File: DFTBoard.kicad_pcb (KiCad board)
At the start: 8 copper layers, 148.5 x 62 mm, 76 parts, among them CON1 AVR-JTAG-10, CON2 AVR-JTAG-10, J1 AUDIO JACK, J2 JACK_TRS_4PINS, J3 AUDIO JACK, J4 AUDIO JACK, J5 USB_A, J6 Micro_SD_Card_Det, SW1 TL6215RF200BDT, U10 APDS-9960, U11 W9751G6KB, U12 W9751G6KB, U7 TLV320AIC3104, U9 VL53L0X

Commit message: passes ERC, about to update footprints to v5 references
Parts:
- removed C63, C67: 10uF, Capacitors_SMD:C_0603
- removed C71, C73: .1uF, Capacitors_SMD:C_0603
- removed C79: 47uF, Capacitors_SMD:C_1210
- removed C80: 4.7uF, Capacitors_SMD:C_0603
- removed D4: LED_RGB, DFTcustom:PLCC6-SM-RGB-LED
- removed NCP1: NCP361, DFTcustom:TSOP-5
- removed R24: 10k, Resistors_SMD:R_0402
- removed the U11 at (196.0, 104.1)
- added C76: 18pF, Capacitor_SMD:C_0402_1005Metric, F.Cu at (223.2, 39.6)
- added C77: 18pF, Capacitor_SMD:C_0402_1005Metric, F.Cu at (223.2, 41.6)
- added C85: 18pF, Capacitor_SMD:C_0402_1005Metric, F.Cu at (225.1, 40.6)
- added C86: 18pF, Capacitor_SMD:C_0402_1005Metric, F.Cu at (230.6, 36.5)
- added D1: LED_RGB, DFTcustom:PLCC6-SM-RGB-LED, F.Cu at (224.6, 117.8)
- added D2: LED_RGB, DFTcustom:PLCC6-SM-RGB-LED, F.Cu at (149.2, 122.5)
- added J7: USB_B, Connector_USB:USB_B_Amphenol_MUSB-D511_Vertical_Rugged, F.Cu at (245.2, 139.8)
- added R27: 1M, Resistor_SMD:R_0402_1005Metric, F.Cu at (223.2, 40.6)
- added R29: 8.06k 1%, Resistor_SMD:R_0402_1005Metric, F.Cu at (225.1, 39.6)
- added R34: 1M, Resistor_SMD:R_0402_1005Metric, F.Cu at (240.7, 25.5)
- added R35: 8.06k 1%, Resistor_SMD:R_0402_1005Metric, F.Cu at (230.6, 35.5)
- added R40: 240 1%, Resistor_SMD:R_0402_1005Metric, F.Cu at (201.2, 99.9)
- added R43: 240 1%, Resistor_SMD:R_0402_1005Metric, F.Cu at (203.1, 99.9)
- added R45: 80.6, Resistor_SMD:R_0402_1005Metric, F.Cu at (205.0, 99.9)
- added R46: 80.6, Resistor_SMD:R_0402_1005Metric, F.Cu at (206.9, 99.9)
- added U13: MT41K256M16HA-125_E, DFTcustom:FBGA-96-DDR3-SDRAM, F.Cu at (195.2, 107.5)
- added U5: xc7z020clg400, Package_BGA:BGA-400_21.0x21.0mm_Layout20x20_P1.0mm, F.Cu at (189.9, 134.3)
- added U9: MIC2025-1YMM, Crystal:Crystal_HC35-U, F.Cu at (214.7, 44.1)
- added Y1: Crystal, Crystal:Crystal_HC35-U, F.Cu at (232.2, 30.0)
- added Y2: Crystal, Crystal:Crystal_HC35-U, F.Cu at (204.7, 44.1)
- R41: renamed from R23; value 10k -> 10k 1%
- U12: value W9751G6KB -> MT41K256M16HA-125_E; footprint DFTcustom:WBGA-84 -> DFTcustom:FBGA-96-DDR3-SDRAM
- moved CONN1 125.5 mm to (170.8, 102.2), turned to 270 degrees
- moved J6 63.9 mm to (242.7, 118.7), turned to 90 degrees
- moved CON1 42.6 mm to (211.2, 156.5)
- moved GT1 22.8 mm to (178.8, 163.8)
- moved CON2 18.1 mm to (220.2, 160.1)
- moved U12 10.1 mm to (185.0, 107.5)
- renumbered C81 to C102, C82 to C104, C83 to C105, C84 to C106, C85 to C107, C34 to C35, C35 to C36, C36 to C39, C37 to C40, C38 to C41, C39 to C43, C40 to C44, C41 to C46, C42 to C50, C43 to C51, C44 to C52, C45 to C53, C46 to C54, C47 to C55, C48 to C56, C49 to C57, C50 to C58, C51 to C59, C52 to C60, C53 to C61, C54 to C62, C58 to C89, C59 to C90, C60 to C91, C61 to C92, C62 to C93, C65 to C94, C66 to C95, C75 to C96, C76 to C97, J6 to J5, J5 to J6, R1 to R13, R2 to R14, R3 to R15, R4 to R16, R5 to R17, R6 to R18, R7 to R19, R8 to R20, R9 to R21, R10 to R22, R19 to R36, R20 to R37, R27 to R44, U9 to U10, U10 to U11, U7 to U6
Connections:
- C102 pad 1: +1.8V -> Net-(C100-Pad1)
- C104 pad 1: +1.8V -> Net-(C100-Pad1)
- C105 pad 1: +1.8V -> Net-(C100-Pad1)
- C106 pad 1: +1.8V -> Net-(C100-Pad1)
- C107 pad 1: +1.8V -> Net-(C100-Pad1)
- C94 pad 1: +1.8V -> +1V35
- C96 pad 1: +1.8V -> +1V35
- CON1 pad 1: (no net) -> AX_TCLK
- CON1 pad 3: (no net) -> AX_TDO
- CON1 pad 5: (no net) -> AX_TMS
- CON1 pad 9: (no net) -> AX_TDI
- CONN2 pad 10: (no net) -> LCD_RST
- CONN2 pad 11: (no net) -> RGB_VSYNC
- CONN2 pad 12: (no net) -> RGB_HSYNC
- CONN2 pad 13: (no net) -> RGB_DOTCLK
- CONN2 pad 14: (no net) -> RGB_DE
- CONN2 pad 15: (no net) -> LCD_D17
- CONN2 pad 16: (no net) -> LCD_D16
- CONN2 pad 17: (no net) -> LCD_D15
- CONN2 pad 18: (no net) -> LCD_D14
- CONN2 pad 19: (no net) -> LCD_D13
- CONN2 pad 20: (no net) -> LCD_D12
- CONN2 pad 21: (no net) -> LCD_D11
- CONN2 pad 22: (no net) -> LCD_D10
- CONN2 pad 23: (no net) -> LCD_D9
- CONN2 pad 24: (no net) -> LCD_D8
- CONN2 pad 25: (no net) -> LCD_D7
- CONN2 pad 26: (no net) -> LCD_D6
- CONN2 pad 27: (no net) -> LCD_D5
- CONN2 pad 28: (no net) -> LCD_D4
- CONN2 pad 29: (no net) -> LCD_D3
- CONN2 pad 30: (no net) -> LCD_D2
- CONN2 pad 31: (no net) -> LCD_D1
- CONN2 pad 32: (no net) -> LCD_D0
- CONN2 pad 33: (no net) -> LCD_SDO
- CONN2 pad 34: (no net) -> LCD_SDI
- CONN2 pad 35: (no net) -> LCD_READ
- CONN2 pad 36: (no net) -> LCD_WRITE
- CONN2 pad 37: (no net) -> LCD_DorI
- CONN2 pad 38: (no net) -> LCD_CS
- CONN2 pad 39: (no net) -> LCD_TE
- CONN2 pad 6: (no net) -> LCD_IM0
- CONN2 pad 7: (no net) -> LCD_IM1
- CONN2 pad 8: (no net) -> LCD_IM2
- CONN2 pad 9: (no net) -> LCD_IM3
- J5 pad 1: (no net) -> SD_D2
- J5 pad 2: (no net) -> SD_D3
- J5 pad 3: (no net) -> SD_CMD
- J5 pad 5: (no net) -> SD_CLK
- J5 pad 7: (no net) -> SD_D0
- J5 pad 8: (no net) -> SD_D1
- J5 pad 9: (no net) -> SD_CD
- J6 pad 1: SPIUSB_VBUS -> (no net)
- R21 pad 1: I2C_SCLK -> I2C3v3_SCLK
- R21 pad 2: +1.8V -> +3V3
- R22 pad 1: I2C_SDIN -> I2C3v3_SDIN
- R22 pad 2: +1.8V -> +3V3
- R41 pad 1: +1.8V -> +1V35
- SW1 pad 2: (no net) -> TEMPO_SW
- U10 pad 10: I2C_SCLK -> (no net)
- U10 pad 9: I2C_SDIN -> (no net)
- U11 pad 1: I2C_SDIN -> (no net)
- U11 pad 2: (no net) -> RF2_IRQ
- U11 pad 7: I2C_SCLK -> (no net)
- U12 pad A1: +1.8V -> +1V35
- U12 pad A2: (no net) -> DDR3_DQ29
- U12 pad A3: GND -> DDR3_DQ31
- U12 pad A7: GND -> DDR3_DQ28
- U12 pad A8: (no net) -> +1V35
- U12 pad A9: +1.8V -> GND
- U12 pad B1: (no net) -> GND
- U12 pad B2: GND -> +1V35
- U12 pad B3: (no net) -> GND
- U12 pad B7: (no net) -> DDR3_DQS3_N
- U12 pad B8: GND -> DDR3_DQ30
- U12 pad B9: (no net) -> GND
- U12 pad C1: +1.8V -> +1V35
- U12 pad C2: (no net) -> DDR3_DQ27
- U12 pad C3: +1.8V -> DDR3_DQ25
- U12 pad C7: +1.8V -> DDR3_DQS3_P
- U12 pad C8: (no net) -> DDR3_DQ26
- U12 pad C9: +1.8V -> +1V35
- U12 pad D1: (no net) -> GND
- U12 pad D2: GND -> +1V35
- U12 pad D3: (no net) -> DDR3_DM3
- U12 pad D7: (no net) -> DDR3_DQ24
- U12 pad D9: (no net) -> +1V35
- U12 pad E1: +1.8V -> GND
- U12 pad E2: (no net) -> GND
- U12 pad E3: GND -> DDR3_DQ16
- U12 pad E7: GND -> DDR3_DM2
- U12 pad E8: (no net) -> GND
- U12 pad E9: +1.8V -> +1V35
- U12 pad F1: (no net) -> +1V35
- U12 pad F2: GND -> DDR3_DQ18
- U12 pad F3: (no net) -> DDR3_DQS2_P
- U12 pad F7: (no net) -> DDR3_DQ17
- U12 pad F8: GND -> DDR3_DQ19
- U12 pad F9: (no net) -> GND
- U12 pad G1: +1.8V -> GND
- U12 pad G2: (no net) -> DDR3_DQ22
- U12 pad G3: +1.8V -> DDR3_DQS2_N
- U12 pad G7: +1.8V -> +1V35
- U12 pad G8: (no net) -> GND
- U12 pad G9: +1.8V -> GND
- U12 pad H1: (no net) -> /DDR3/VREF
- U12 pad H2: GND -> +1V35
- U12 pad H3: (no net) -> DDR3_DQ20
- U12 pad H7: (no net) -> DDR3_DQ23
- U12 pad H8: GND -> DDR3_DQ21
- U12 pad H9: (no net) -> +1V35
- U12 pad J1: +1.8V -> (no net)
- U12 pad J2: /DDR3/VREF -> GND
- U12 pad J3: GND -> DDR3_RAS#
- U12 pad J7: GND -> DDR3_CK_P
- U12 pad J8: DDR3_CK_P -> GND
- U12 pad J9: +1.8V -> (no net)
- U12 pad K2: DDR3_CKE -> +1V35
- U12 pad K3: DDR3_WE# -> DDR3_CAS#
- U12 pad K7: DDR3_RAS# -> DDR3_CK_N
- U12 pad K8: DDR3_CK_N -> +1V35
- U12 pad K9: DDR3_ODT -> DDR3_CKE
- U12 pad L2: DDR3_BA0 -> DDR3_CS#
- U12 pad L3: DDR3_BA1 -> DDR3_WE#
- U12 pad L7: DDR3_CAS# -> DDR3_A10
- U12 pad L8: DDR3_CS -> Net-(R40-Pad1)
- U12 pad M2: DDR3_A10 -> DDR3_BA0
- U12 pad M3: DDR3_A1 -> DDR3_BA2
- U12 pad M7: DDR3_A2 -> (no net)
- U12 pad M8: DDR3_A0 -> /DDR3/VREF
- U12 pad M9: +1.8V -> GND
- U12 pad N1: GND -> +1V35
- U12 pad N3: DDR3_A5 -> DDR3_A0
- U12 pad N7: DDR3_A6 -> DDR3_A12
- U12 pad N8: DDR3_A4 -> DDR3_BA1
- U12 pad P2: DDR3_A7 -> DDR3_A5
- U12 pad P3: DDR3_A9 -> DDR3_A2
- U12 pad P7: DDR3_A11 -> DDR3_A1
- U12 pad P8: DDR3_A8 -> DDR3_A4
- U12 pad R1: +1.8V -> +1V35
- U12 pad R2: DDR3_A12 -> DDR3_A7
- U12 pad R3: (no net) -> DDR3_A9
- U12 pad R7: (no net) -> DDR3_A11
- U12 pad R8: (no net) -> DDR3_A6
- U6 pad 1: (no net) -> I2S_MCLK
- U6 pad 2: (no net) -> I2S_BCLK
- U6 pad 3: (no net) -> I2S_LRCLK
- U6 pad 4: (no net) -> I2S_DACSD
- U6 pad 5: (no net) -> I2S_ADCSD

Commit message: random updates
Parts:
- removed CON2: AVR-JTAG-10, DFTcustom:XilinxJTAG
- removed the J5 at (247.8, 103.2)
- removed the R37 at (143.6, 128.4)
- removed the R40 at (201.2, 99.9)
- removed the R41 at (205.0, 102.6)
- removed the U13 at (195.2, 107.5)
- added C1: .47uF, Capacitor_SMD:C_0402_1005Metric, B.Cu at (165.2, 141.2)
- added C10: 10uF, Capacitor_SMD:C_0603_1608Metric, F.Cu at (160.0, 96.5)
- added C100: 4.7uF, Capacitor_SMD:C_0402_1005Metric, F.Cu at (217.1, 117.4)
- added C101: .47uF, Capacitor_SMD:C_0402_1005Metric, B.Cu at (185.4, 112.8)
- added C103: .47uF, Capacitor_SMD:C_0402_1005Metric, B.Cu at (191.4, 114.8)
- added C108: 4.7uF, Capacitor_SMD:C_0402_1005Metric, B.Cu at (134.8, 145.1)
- added C109: .1uF, Capacitor_SMD:C_0402_1005Metric, F.Cu at (150.4, 138.4)
- added C11: 10uF, Capacitor_SMD:C_0603_1608Metric, B.Cu at (165.2, 150.8)
- added C110: 4.7uF, Capacitor_SMD:C_0402_1005Metric, B.Cu at (150.4, 138.4)
- added C111: .1uF, Capacitor_SMD:C_0402_1005Metric, B.Cu at (150.4, 136.2)
- added C112: 4.7uF, Capacitor_SMD:C_0402_1005Metric, F.Cu at (150.4, 136.2)
- added C113: 47uF, Capacitor_SMD:C_1210_3225Metric, F.Cu at (176.2, 130.5)
- added C114: 4.7uF, Capacitor_SMD:C_0402_1005Metric, F.Cu at (230.4, 170.4)
- added C115: 4.7uF, Capacitor_SMD:C_0402_1005Metric, B.Cu at (216.4, 130.5)
- added C116: .47uF, Capacitor_SMD:C_0402_1005Metric, B.Cu at (198.0, 127.4)
- added C117: .47uF, Capacitor_SMD:C_0402_1005Metric, F.Cu at (232.3, 170.4)
- added C118: .47uF, Capacitor_SMD:C_0402_1005Metric, F.Cu at (230.4, 172.4)
- added C119: .47uF, Capacitor_SMD:C_0402_1005Metric, B.Cu at (199.4, 125.2)
- added C12: 100uF, Capacitor_SMD:C_1210_3225Metric, F.Cu at (214.1, 135.2)
- added C120: .01uF, Capacitor_SMD:C_0402_1005Metric, B.Cu at (218.2, 120.7)
- added C121: .47uF, Capacitor_SMD:C_0402_1005Metric, B.Cu at (210.2, 130.0)
- added C122: 4.7uF, Capacitor_SMD:C_0402_1005Metric, B.Cu at (208.4, 124.0)
- added C123: 100uF, Capacitor_SMD:C_1210_3225Metric, F.Cu at (216.4, 126.8)
- added C13: 10uF, Capacitor_SMD:C_0603_1608Metric, F.Cu at (154.0, 147.2)
- added C14: .47uF, Capacitor_SMD:C_0402_1005Metric, F.Cu at (218.3, 171.4)
- added C15: .47uF, Capacitor_SMD:C_0402_1005Metric, B.Cu at (202.6, 130.0)
- added C16: 10uF, Capacitor_SMD:C_0603_1608Metric, F.Cu at (244.0, 101.5)
- added C17: .47uF, Capacitor_SMD:C_0402_1005Metric, F.Cu at (220.2, 170.4)
- added C18: .47uF, Capacitor_SMD:C_0402_1005Metric, B.Cu at (197.2, 129.6)
- added C19: 4.7uF, Capacitor_SMD:C_0402_1005Metric, F.Cu at (171.2, 125.7)
- added C2: 10uF, Capacitor_SMD:C_0603_1608Metric, F.Cu at (168.8, 152.2)
- added C20: 4.7uF, Capacitor_SMD:C_0402_1005Metric, B.Cu at (201.6, 129.2)
- added C21: 10uF, Capacitor_SMD:C_0603_1608Metric, F.Cu at (238.0, 103.6)
- added C22: 330uF, Capacitor_SMD:C_1206_3216Metric, F.Cu at (218.4, 137.0)
- added C23: .47uF, Capacitor_SMD:C_0402_1005Metric, B.Cu at (197.2, 126.4)
- added C24: 4.7uF, Capacitor_SMD:C_0402_1005Metric, F.Cu at (204.6, 140.2)
- added C25: 100uF, Capacitor_SMD:C_1210_3225Metric, F.Cu at (176.2, 119.5)
- added C26: 10uF, Capacitor_SMD:C_0603_1608Metric, B.Cu at (161.2, 142.5)
- added C27: 4.7uF, Capacitor_SMD:C_0402_1005Metric, B.Cu at (215.3, 130.5)
- added C28: 100uF, Capacitor_SMD:C_1210_3225Metric, F.Cu at (176.2, 125.5)
- added C29: .47uF, Capacitor_SMD:C_0402_1005Metric, B.Cu at (203.6, 125.8)
- added C3: 10uF, Capacitor_SMD:C_0603_1608Metric, B.Cu at (164.6, 104.1)
- added C30: .47uF, Capacitor_SMD:C_0402_1005Metric, B.Cu at (203.6, 124.8)
- added C31: .47uF, Capacitor_SMD:C_0402_1005Metric, B.Cu at (197.2, 130.6)
- added C32: 47uF, Capacitor_SMD:C_0805_2012Metric, B.Cu at (178.4, 136.4)
- added C33: 10uF, Capacitor_SMD:C_0603_1608Metric, B.Cu at (214.0, 127.8)
- added C34: .47uF, Capacitor_SMD:C_0402_1005Metric, F.Cu at (220.2, 174.4)
- added C37: 1uF, Capacitor_SMD:C_0402_1005Metric, F.Cu at (134.7, 135.6)
- added C38: 1uF, Capacitor_SMD:C_0402_1005Metric, F.Cu at (140.2, 121.1)
- added C4: .47uF, Capacitor_SMD:C_0402_1005Metric, B.Cu at (196.4, 125.4)
- added C42: 4.7uF, Capacitor_SMD:C_0402_1005Metric, F.Cu at (144.2, 123.3)
- added C45: 1uF, Capacitor_SMD:C_0402_1005Metric, F.Cu at (136.9, 120.8)
- added C47: .47uF, Capacitor_SMD:C_0402_1005Metric, B.Cu at (191.1, 155.5)
- added C48: 220uF Tant., Capacitor_Tantalum_SMD:CP_EIA-3528-12_Kemet-T, F.Cu at (138.8, 100.9)
- added C49: 220uF Tant., Capacitor_Tantalum_SMD:CP_EIA-3528-12_Kemet-T, F.Cu at (146.8, 109.0)
- added C5: 4.7uF, Capacitor_SMD:C_0402_1005Metric, B.Cu at (197.2, 128.6)
- added C6: 100uF, Capacitor_SMD:C_1210_3225Metric, F.Cu at (186.0, 141.0)
- added C63: .1uF, Capacitor_SMD:C_0402_1005Metric, F.Cu at (138.7, 129.9)
- added C64: .1uF, Capacitor_SMD:C_0402_1005Metric, F.Cu at (135.3, 111.2)
- added C65: .47uF, Capacitor_SMD:C_0402_1005Metric, B.Cu at (198.0, 132.0)
- added C66: 4.7uF, Capacitor_SMD:C_0402_1005Metric, F.Cu at (172.2, 116.8)
- added C67: 100uF, Capacitor_SMD:C_1210_3225Metric, F.Cu at (179.4, 138.6)
- added C68: .1uF, Capacitor_SMD:C_0402_1005Metric, B.Cu at (225.8, 121.0)
- added C69: 2.2uF, Capacitor_SMD:C_0402_1005Metric, F.Cu at (228.0, 116.2)
- added C7: 47uF, Capacitor_SMD:C_0805_2012Metric, B.Cu at (214.7, 98.9)
- added C70: .1uF, Capacitor_SMD:C_0402_1005Metric, B.Cu at (220.2, 115.8)
- added C71: .1uF, Capacitor_SMD:C_0402_1005Metric, B.Cu at (222.5, 121.0)
- added C72: .1uF, Capacitor_SMD:C_0402_1005Metric, B.Cu at (238.0, 111.2)
- added C73: 100uF, Capacitor_SMD:C_1210_3225Metric, F.Cu at (245.2, 118.5)
- added C74: 100uF, Capacitor_SMD:C_1210_3225Metric, F.Cu at (248.8, 118.5)
- added C77: .1uF, Capacitor_SMD:C_0402_1005Metric, B.Cu at (227.8, 121.0)
- added C78: .47uF, Capacitor_SMD:C_0402_1005Metric, F.Cu at (229.1, 116.3)
- added C79: .1uF, Capacitor_SMD:C_0402_1005Metric, F.Cu at (224.4, 137.1)
- added C8: .47uF, Capacitor_SMD:C_0402_1005Metric, B.Cu at (199.4, 129.2)
- added C80: 2.2uF, Capacitor_SMD:C_0402_1005Metric, F.Cu at (228.5, 131.2)
- added C81: .1uF, Capacitor_SMD:C_0402_1005Metric, F.Cu at (226.4, 137.1)
- added C82: .1uF, Capacitor_SMD:C_0402_1005Metric, B.Cu at (226.4, 137.1)
- added C83: 4.7uF, Capacitor_SMD:C_0402_1005Metric, F.Cu at (250.5, 140.8)
- added C86: .1uF, Capacitor_SMD:C_0402_1005Metric, B.Cu at (228.3, 119.3)
- added C87: .47uF, Capacitor_SMD:C_0402_1005Metric, F.Cu at (225.4, 128.8)
- added C88: .1uF, Capacitor_SMD:C_0402_1005Metric, F.Cu at (142.0, 131.6)
- added C9: 4.7uF, Capacitor_SMD:C_0402_1005Metric, B.Cu at (200.6, 130.0)
- added C98: .01uF, Capacitor_SMD:C_0402_1005Metric, B.Cu at (217.7, 105.0)
- added C99: 100uF, Capacitor_SMD:C_1210_3225Metric, B.Cu at (217.7, 99.0)
- added D3: BLUE LED, Capacitor_SMD:C_0603_1608Metric, F.Cu at (233.0, 110.9)
- added D4: BLUE LED, Capacitor_SMD:C_0603_1608Metric, F.Cu at (216.8, 142.2)
- added D5: BLUE LED, Capacitor_SMD:C_0603_1608Metric, F.Cu at (221.8, 142.2)
- added D6: BLUE LED, Capacitor_SMD:C_0603_1608Metric, F.Cu at (226.8, 142.2)
- added FB1: 120Ω @ 100 MHz, size 0603, Capacitor_SMD:C_0603_1608Metric, B.Cu at (219.0, 130.0)
- added J1: PJ-102A, PJ-102A:CUI_PJ-102A, B.Cu at (247.4, 101.5)
- added J8: Micro_SD_Card_Det, DFTcustom:AMPHENOL-114-00841-68, B.Cu at (207.6, 148.0)
- added J9: HDMI_A, DFTcustom:10029449-111RLF, B.Cu at (187.8, 152.5)
- added JP1: Jumper_3_Open, DFTcustom:JUMPER_3PIN, F.Cu at (238.0, 131.8)
- added L1: 2.2uH, Capacitor_SMD:C_1812_4532Metric, B.Cu at (171.2, 107.8)
- added L2: 2.2uH, Capacitor_SMD:C_1812_4532Metric, B.Cu at (163.9, 96.5)
- added L3: 2.2uH, Capacitor_SMD:C_1812_4532Metric, B.Cu at (168.0, 146.5)
- added L4: 2.2uH, Capacitor_SMD:C_1812_4532Metric, B.Cu at (161.2, 146.5)
- added Q1: IRLML2502, Package_TO_SOT_SMD:SOT-23, F.Cu at (241.8, 128.8)
- added Q10: IRLML2502, Package_TO_SOT_SMD:SOT-23, B.Cu at (226.1, 141.2)
- added Q2: IRLML2502, Package_TO_SOT_SMD:SOT-23, F.Cu at (143.2, 141.2)
- added Q3: IRLML2502, Package_TO_SOT_SMD:SOT-23, B.Cu at (234.5, 124.2)
- added Q4: IRLML2502, Package_TO_SOT_SMD:SOT-23, B.Cu at (148.0, 124.8)
- added Q5: IRLML2502, Package_TO_SOT_SMD:SOT-23, B.Cu at (236.5, 120.5)
- added Q6: IRLML2502, Package_TO_SOT_SMD:SOT-23, B.Cu at (149.6, 128.6)
- added Q7: IRLML2502, Package_TO_SOT_SMD:SOT-23, F.Cu at (195.8, 98.0)
- added Q8: IRLML2502, Package_TO_SOT_SMD:SOT-23, B.Cu at (216.1, 141.2)
- added Q9: IRLML2502, Package_TO_SOT_SMD:SOT-23, B.Cu at (221.1, 141.2)
- added R1: 100k, Resistor_SMD:R_0402_1005Metric, B.Cu at (168.2, 143.8)
- added R10: 4.7k, Resistor_SMD:R_0402_1005Metric, F.Cu at (224.0, 172.4)
- added R100: 24.9 1%, Resistor_SMD:R_0402_1005Metric, B.Cu at (212.8, 120.2)
- added R11: 100, Resistor_SMD:R_0402_1005Metric, F.Cu at (244.5, 129.7)
- added R12: 100, Resistor_SMD:R_0402_1005Metric, F.Cu at (142.5, 138.9)
- added R2: 100k, Resistor_SMD:R_0402_1005Metric, B.Cu at (153.2, 146.2)
- added R23: 100, Resistor_SMD:R_0402_1005Metric, B.Cu at (148.0, 121.5)
- added R24: 150, Resistor_SMD:R_0402_1005Metric, B.Cu at (150.0, 121.5)
- added R25: 4.7k, Resistor_SMD:R_0402_1005Metric, F.Cu at (178.8, 142.1)
- added R26: 4.7k, Resistor_SMD:R_0402_1005Metric, F.Cu at (180.8, 142.1)
- added R27: 100k, Resistor_SMD:R_0402_1005Metric, F.Cu at (129.0, 113.0)
- added R28: 100k, Resistor_SMD:R_0402_1005Metric, F.Cu at (140.8, 108.2)
- added R29: 100k, Resistor_SMD:R_0402_1005Metric, F.Cu at (137.3, 130.5)
- added R3: 100k, Resistor_SMD:R_0402_1005Metric, B.Cu at (162.6, 103.9)
- added R30: 49.9k, Resistor_SMD:R_0402_1005Metric, F.Cu at (137.7, 132.0)
- added R31: 49.9k, Resistor_SMD:R_0402_1005Metric, F.Cu at (143.3, 108.5)
- added R32: 49.9k, Resistor_SMD:R_0402_1005Metric, F.Cu at (133.8, 113.6)
- added R33: 10k, Resistor_SMD:R_0402_1005Metric, F.Cu at (212.3, 128.9)
- added R34: 47, Resistor_SMD:R_0402_1005Metric, F.Cu at (211.1, 135.3)
- added R35: 150, Resistor_SMD:R_0402_1005Metric, F.Cu at (232.2, 112.8)
- added R39: 10k, Resistor_SMD:R_0402_1005Metric, F.Cu at (228.5, 132.2)
- added R4: 100k, Resistor_SMD:R_0402_1005Metric, B.Cu at (154.1, 103.3)
- added R42: 10k, Resistor_SMD:R_0402_1005Metric, B.Cu at (145.8, 129.4)
- added R47: 10k 1%, Resistor_SMD:R_0402_1005Metric, F.Cu at (186.2, 106.2)
- added R48: 10k 1%, Resistor_SMD:R_0402_1005Metric, F.Cu at (186.2, 108.2)
- added R49: 240 1%, Resistor_SMD:R_0402_1005Metric, F.Cu at (214.4, 110.4)
- added R5: 100k, Resistor_SMD:R_0402_1005Metric, F.Cu at (212.3, 126.8)
- added R50: 100, Resistor_SMD:R_0402_1005Metric, B.Cu at (194.1, 105.6)
- added R51: 40.2 1%, Resistor_SMD:R_0402_1005Metric, F.Cu at (220.1, 112.8)
- added R52: 40.2 1%, Resistor_SMD:R_0402_1005Metric, F.Cu at (216.3, 111.9)
- added R53: 40.2 1%, Resistor_SMD:R_0402_1005Metric, F.Cu at (216.3, 112.8)
- added R54: 40.2 1%, Resistor_SMD:R_0402_1005Metric, F.Cu at (214.4, 113.3)
- added R55: 40.2 1%, Resistor_SMD:R_0402_1005Metric, F.Cu at (218.2, 112.8)
- added R56: 40.2 1%, Resistor_SMD:R_0402_1005Metric, F.Cu at (216.3, 113.8)
- added R57: 40.2 1%, Resistor_SMD:R_0402_1005Metric, F.Cu at (216.3, 114.8)
- added R58: 40.2 1%, Resistor_SMD:R_0402_1005Metric, F.Cu at (218.2, 113.8)
- added R59: 40.2 1%, Resistor_SMD:R_0402_1005Metric, F.Cu at (214.4, 114.3)
- added R6: 10k, Resistor_SMD:R_0402_1005Metric, B.Cu at (158.2, 103.4)
- added R60: 40.2 1%, Resistor_SMD:R_0402_1005Metric, F.Cu at (218.2, 114.8)
- added R61: 40.2 1%, Resistor_SMD:R_0402_1005Metric, F.Cu at (216.3, 109.9)
- added R62: 40.2 1%, Resistor_SMD:R_0402_1005Metric, F.Cu at (218.2, 111.8)
- added R63: 40.2 1%, Resistor_SMD:R_0402_1005Metric, F.Cu at (220.1, 113.8)
- added R64: 40.2 1%, Resistor_SMD:R_0402_1005Metric, F.Cu at (214.4, 116.3)
- added R65: 40.2 1%, Resistor_SMD:R_0402_1005Metric, F.Cu at (214.4, 115.3)
- added R66: 40.2 1%, Resistor_SMD:R_0402_1005Metric, F.Cu at (218.2, 110.9)
- added R67: 40.2 1%, Resistor_SMD:R_0402_1005Metric, F.Cu at (214.4, 112.3)
- added R68: 40.2 1%, Resistor_SMD:R_0402_1005Metric, F.Cu at (216.3, 110.9)
- added R69: 40.2 1%, Resistor_SMD:R_0402_1005Metric, F.Cu at (214.4, 108.4)
- added R7: 240 1%, Resistor_SMD:R_0402_1005Metric, B.Cu at (158.5, 101.9)
- added R70: 40.2 1%, Resistor_SMD:R_0402_1005Metric, F.Cu at (218.2, 109.9)
- added R71: 40.2 1%, Resistor_SMD:R_0402_1005Metric, F.Cu at (216.4, 108.9)
- added R72: 40.2 1%, Resistor_SMD:R_0402_1005Metric, F.Cu at (214.4, 109.4)
- added R73: 40.2 1%, Resistor_SMD:R_0402_1005Metric, F.Cu at (214.4, 111.3)
- added R74: 4.7k, Resistor_SMD:R_0402_1005Metric, F.Cu at (214.4, 117.3)
- added R75: 80.6, Resistor_SMD:R_0402_1005Metric, F.Cu at (207.0, 117.2)
- added R76: 80.6, Resistor_SMD:R_0402_1005Metric, F.Cu at (202.0, 116.5)
- added R77: 1k, Resistor_SMD:R_0402_1005Metric, F.Cu at (215.1, 139.8)
- added R78: 150, Resistor_SMD:R_0402_1005Metric, F.Cu at (217.8, 140.5)
- added R79: 1k, Resistor_SMD:R_0402_1005Metric, F.Cu at (220.1, 139.8)
- added R8: 4.7k, Resistor_SMD:R_0402_1005Metric, B.Cu at (158.5, 100.9)
- added R80: 150, Resistor_SMD:R_0402_1005Metric, F.Cu at (222.8, 140.5)
- added R81: 10k, Resistor_SMD:R_0402_1005Metric, F.Cu at (210.3, 97.7)
- added R82: 10k, Resistor_SMD:R_0402_1005Metric, B.Cu at (150.5, 115.3)
- added R83: 10k, Resistor_SMD:R_0402_1005Metric, B.Cu at (148.5, 115.4)
- added R84: 10k, Resistor_SMD:R_0402_1005Metric, B.Cu at (148.4, 114.4)
- added R85: 1k, Resistor_SMD:R_0402_1005Metric, F.Cu at (225.1, 139.8)
- added R86: 150, Resistor_SMD:R_0402_1005Metric, F.Cu at (227.8, 140.5)
- added R87: 33, Resistor_SMD:R_0402_1005Metric, B.Cu at (150.4, 113.8)
- added R88: 33, Resistor_SMD:R_0402_1005Metric, B.Cu at (148.5, 113.3)
- added R89: 33, Resistor_SMD:R_0402_1005Metric, B.Cu at (150.4, 112.8)
- added R9: 4.7k, Resistor_SMD:R_0402_1005Metric, F.Cu at (222.1, 173.4)
- added R90: 33, Resistor_SMD:R_0402_1005Metric, B.Cu at (148.5, 112.3)
- added R91: 20k, Resistor_SMD:R_0402_1005Metric, F.Cu at (211.2, 123.6)
- added R92: 20k, Resistor_SMD:R_0402_1005Metric, F.Cu at (212.3, 124.8)
- added R93: 20k, Resistor_SMD:R_0402_1005Metric, F.Cu at (220.2, 122.6)
- added R94: 20k, Resistor_SMD:R_0402_1005Metric, F.Cu at (217.6, 123.4)
- added R95: 20k, Resistor_SMD:R_0402_1005Metric, F.Cu at (214.2, 124.0)
- added R96: 20k, Resistor_SMD:R_0402_1005Metric, F.Cu at (212.3, 125.8)
- added R97: 20k, Resistor_SMD:R_0402_1005Metric, F.Cu at (211.2, 122.5)
- added R98: 4.7k, Resistor_SMD:R_0402_1005Metric, B.Cu at (218.6, 122.2)
- added R99: 47k, Resistor_SMD:R_0402_1005Metric, F.Cu at (174.0, 139.3)
- added U1: LM3880, Package_TO_SOT_SMD:SOT-23-6, B.Cu at (168.2, 141.2)
- added U10: USB3320, Package_DFN_QFN:QFN-32-1EP_5x5mm_P0.5mm_EP3.1x3.1mm, F.Cu at (224.0, 117.0)
- added U11: MIC2025-1YMM, SOP65P490X110-8N:SOP65P490X110-8N, F.Cu at (238.0, 111.2)
- added U12: USB3320, Package_DFN_QFN:QFN-32-1EP_5x5mm_P0.5mm_EP3.1x3.1mm, F.Cu at (224.2, 133.2)
- added U16: MT41K256M16HA-125_E, DFTcustom:FBGA-96-DDR3-SDRAM, F.Cu at (207.0, 108.5)
- added U17: FTDITypeUART, DFTcustom:FTDI_CONN, F.Cu at (179.6, 96.8)
- added U18: ABRACON-ASDMB, XTAL_ASDMB-24.000MHZ-LC-T:XTAL_ASDMB-24.000MHZ-LC-T, B.Cu at (215.8, 121.0)
- added U19: S25FL256SAGNFI001, DFTcustom:WSON-8, F.Cu at (220.0, 125.2)
- added U2: LM3880, Package_TO_SOT_SMD:SOT-23-6, F.Cu at (188.6, 149.8)
- added U20: xc7z020clg484, DFTcustom:BGA-484_19.0x19.0mm_Layout22x22_P0.80mm_dia0.40mm, F.Cu at (200.0, 128.0)
- added U3: SC189 - 1.0V, Package_TO_SOT_SMD:SOT-23-5, B.Cu at (168.0, 151.0)
- added U4: SC189 - 3.3V, Package_TO_SOT_SMD:SOT-23-5, B.Cu at (163.9, 101.0)
- added U7: SC189 - 1.8V, Package_TO_SOT_SMD:SOT-23-5, B.Cu at (156.0, 146.2)
- C102, C46: value 4.7uF -> .47uF; footprint Capacitors_SMD:C_0603 -> Capacitor_SMD:C_0402_1005Metric; moved to B.Cu
- C104, C36, C40, C52, C53, C92, C94, C95, C96, C97: footprint Capacitors_SMD:C_0603 -> Capacitor_SMD:C_0402_1005Metric
- C105, C106: value .47uF -> .01uF; footprint Capacitors_SMD:C_0603 -> Capacitor_SMD:C_0402_1005Metric
- C107: value .47uF -> .1uF; footprint Capacitors_SMD:C_0603 -> Capacitor_SMD:C_0402_1005Metric; moved to F.Cu
- C35: footprint Capacitors_SMD:C_0402 -> Capacitor_SMD:C_0402_1005Metric
- C39: value 1uF -> .1uF; footprint Capacitors_SMD:C_0603 -> Capacitor_SMD:C_0402_1005Metric; moved to B.Cu
- C41: value .1uF -> 10uF; footprint Capacitors_SMD:C_0603 -> Capacitor_SMD:C_0603_1608Metric
- C43, C62: footprint Capacitors_SMD:C_0603 -> Capacitor_SMD:C_0402_1005Metric; moved to B.Cu
- C44, C91: value 10uF -> 1uF; footprint Capacitors_SMD:C_0603 -> Capacitor_SMD:C_0402_1005Metric
- C50: value 1uF -> .47uF; footprint Capacitors_SMD:C_0603 -> Capacitor_SMD:C_0402_1005Metric; moved to B.Cu
- C51, C54: footprint Capacitors_SMD:C_0603 -> Capacitor_SMD:C_0603_1608Metric
- C55: value .1uF -> .47uF; footprint Capacitors_SMD:C_0603 -> Capacitor_SMD:C_0402_1005Metric
- C56: value 10uF -> .1uF; footprint Capacitors_SMD:C_0603 -> Capacitor_SMD:C_0402_1005Metric; moved to B.Cu
- C57: value 10uF -> 4.7uF; footprint Capacitors_SMD:C_0603 -> Capacitor_SMD:C_0402_1005Metric
- C58: value .1uF -> 10uF; footprint Capacitors_SMD:C_0603 -> Capacitor_SMD:C_0603_1608Metric; moved to F.Cu
- C59: value 220uF Tant. -> 4.7uF; footprint Capacitors_Tantalum_SMD:CP_Tantalum_Case-T_EIA-3528-12_Reflow -> Capacitor_SMD:C_0402_1005Metric; moved to B.Cu
- C60: value 220uF Tant. -> 10uF; footprint Capacitors_Tantalum_SMD:CP_Tantalum_Case-T_EIA-3528-12_Reflow -> Capacitor_SMD:C_0603_1608Metric; moved to B.Cu
- C61: value .1uF -> 47uF; footprint Capacitors_SMD:C_0603 -> Capacitor_SMD:C_0805_2012Metric; moved to B.Cu
- C89: value .1uF -> 4.7uF; footprint Capacitors_SMD:C_0603 -> Capacitor_SMD:C_0402_1005Metric; moved to B.Cu
- C90: value 4.7uF -> 10uF; footprint Capacitors_SMD:C_0603 -> Capacitor_SMD:C_0603_1608Metric; moved to F.Cu
- C93: value 1uF -> .01uF; footprint Capacitors_SMD:C_0603 -> Capacitor_SMD:C_0402_1005Metric; moved to B.Cu
- CONN1, J6, J7: moved to B.Cu
- R13, R15, R16: value 100k -> 100; footprint Resistors_SMD:R_0402 -> Resistor_SMD:R_0402_1005Metric; moved to B.Cu
- R14: value 49.9k -> 100; footprint Resistors_SMD:R_0402 -> Resistor_SMD:R_0402_1005Metric; moved to B.Cu
- R17, R18: footprint Resistors_SMD:R_0402 -> Resistor_SMD:R_0402_1005Metric
- R19, R20: value 49.9k -> 100; footprint Resistors_SMD:R_0402 -> Resistor_SMD:R_0402_1005Metric
- R21: value 4.7k -> 150; footprint Resistors_SMD:R_0402 -> Resistor_SMD:R_0402_1005Metric
- R22: value 4.7k -> 100; footprint Resistors_SMD:R_0402 -> Resistor_SMD:R_0402_1005Metric
- R36: footprint Resistors_SMD:R_0402 -> Resistor_SMD:R_0402_1005Metric; moved to F.Cu
- R43: value 240 1% -> 10k; moved to B.Cu
- R44: value 100 -> 10k; footprint Resistors_SMD:R_0402 -> Resistor_SMD:R_0402_1005Metric; moved to F.Cu
- R45: value 80.6 -> 150
- R46: value 80.6 -> 240 1%
- U5: value xc7z020clg400 -> TLV62080DSGx; footprint Package_BGA:BGA-400_21.0x21.0mm_Layout20x20_P1.0mm -> Package_SON:WSON-8-1EP_2x2mm_P0.5mm_EP0.9x1.6mm; moved to B.Cu
- U6: value TLV320AIC3104 -> LM1085-5.0; footprint Housings_DFN_QFN:QFN-32-1EP_5x5mm_Pitch0.5mm -> Package_TO_SOT_SMD:TO-263-3_TabPin2
- U9: value MIC2025-1YMM -> TLV320AIC3104; footprint Crystal:Crystal_HC35-U -> Package_DFN_QFN:QFN-32-1EP_5x5mm_P0.5mm_EP3.65x3.65mm
- Y1, Y2: value Crystal -> ABM3-24.000MHZ-D2Y-T; footprint Crystal:Crystal_HC35-U -> ABM3-12.000MHZ-B2-T:XTAL500X320X130N; moved to B.Cu
- moved C43 109.0 mm to (233.8, 128.2), turned to 0 degrees
- moved R15 106.6 mm to (235.5, 117.8), turned to 90 degrees
- moved U9 104.7 mm to (138.4, 115.8), turned to 180 degrees
- moved R13 102.7 mm to (233.8, 126.5)
- moved R40 102.4 mm to (225.4, 126.7)
- moved R19 97.3 mm to (231.1, 127.6), turned to 0 degrees
- moved SW1 96.9 mm to (202.2, 93.0), turned to 180 degrees
- moved R41 94.7 mm to (228.5, 130.2)
- moved C85 91.3 mm to (227.0, 127.8)
- moved R20 90.9 mm to (228.3, 124.0), turned to 0 degrees
- moved GT1 89.9 mm to (250.0, 109.0)
- moved U6 88.4 mm to (228.2, 102.5)
- moved C84 87.2 mm to (223.8, 127.8), turned to 180 degrees
- moved Y2 86.2 mm to (225.4, 127.8)
- moved R36 83.1 mm to (230.7, 116.3), turned to 0 degrees
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- renumbered C76 to C75, C77 to C76, C85 to C84, C86 to C85, J1 to J2, J4 to J3, J3 to J4, J2 to J5, R27 to R37, R29 to R38, R34 to R40, R35 to R41, U10 to U13, U11 to U14, U12 to U15
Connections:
- C102 pad 1: Net-(C100-Pad1) -> +1V35
- C104 pad 1: Net-(C100-Pad1) -> +1V35
- C105 pad 1: Net-(C100-Pad1) -> /DDR3/VREF
- C106 pad 1: Net-(C100-Pad1) -> /DDR3/VREF
- C107 pad 1: Net-(C100-Pad1) -> +3V3
- C39 pad 1: /Audio/JACK_INC_P -> GND
- C39 pad 2: /Audio/JACK_IN_P -> +1V8
- C40 pad 1: /Audio/SIG_F -> /Audio/JACK_INC_N
- C40 pad 2: /Audio/SIGC_F -> /Audio/JACK_IN_N
- C41 pad 2: +1.8V -> +1V8
- C43 pad 1: /Audio/JACK_INC_N -> +5V
- C43 pad 2: /Audio/JACK_IN_N -> GND
- C44 pad 1: GND -> +5V
- C44 pad 2: +1.8V -> GND
- C46 pad 1: /Audio/MICBIAS -> +3V3
- C46 pad 2: GNDA -> GND
- C50 pad 1: GNDA -> +3V3
- C50 pad 2: Net-(C50-Pad2) -> GND
- C51 pad 1: +1.8V -> +1V8
- C53 pad 1: +1.8V -> +1V8
- C55 pad 1: GNDA -> +3V3
- C55 pad 2: +3V3 -> GND
- C57 pad 2: GNDA -> GND
- C58 pad 1: +3V3 -> GNDA
- C58 pad 2: GNDA -> +3V3
- C59 pad 1: /Audio/HPRCOM_N -> +3V3
- C59 pad 2: /Audio/HPRCOM_MC -> GND
- C60 pad 1: /Audio/HPRCOM_P -> +3V3
- C60 pad 2: /Audio/HPRCOM_PC -> GNDA
- C61 pad 1: JD_ROUT -> +3V3
- C62 pad 1: JD_LOUT -> +3V3
- C62 pad 2: GND -> GNDA
- C90 pad 1: +3V3 -> GND
- C90 pad 2: GND -> +3V3
- C93 pad 1: GND -> /DDR3/VREF
- C93 pad 2: +3V3 -> GND
- CON1 pad 4: +1.8V -> +1V8
- CONN1 pad 2: I2C_SDIN -> I2C33_SDA
- CONN1 pad 3: I2C_SCLK -> I2C33_SCLK
- CONN1 pad 4: (no net) -> TOUCH_RST#
- CONN1 pad 5: (no net) -> TOUCH_INT#
- CONN2 pad 2: (no net) -> Net-(CONN2-Pad2)
- CONN2 pad 3: (no net) -> Net-(CONN2-Pad3)
- CONN2 pad 4: (no net) -> Net-(CONN2-Pad4)
- CONN2 pad 40: +1.8V -> +1V8
- CONN2 pad 41: +1.8V -> +1V8
- CONN2 pad 5: (no net) -> Net-(CONN2-Pad5)
- D2 pad 1: /Audio/LED_1RC -> /Audio/LED_2RC
- D2 pad 2: /Audio/LED_1GC -> /Audio/LED_2GC
- D2 pad 3: /Audio/LED_1BC -> /Audio/LED_2BC
- D2 pad 4: /Audio/LED_1BA -> /Audio/LED_2BA
- D2 pad 5: /Audio/LED_1GA -> /Audio/LED_2GA
- D2 pad 6: /Audio/LED_1RA -> /Audio/LED_2RA
- J3 pad R: /Audio/LOUT_P -> LOUT_N
- J3 pad T: /Audio/LOUT_N -> LOUT_P
- J4 pad R: /Audio/ROUT_P -> ROUT_N
- J4 pad T: /Audio/ROUT_N -> ROUT_P
- J6 pad 1: (no net) -> USBH_VBUS
- J6 pad 2: (no net) -> USBH_D_N
- J6 pad 3: (no net) -> USBH_D_P
- J7 pad 1: (no net) -> USBD_VBUS
- J7 pad 2: (no net) -> USBD_D_N
- J7 pad 3: (no net) -> USBD_D_P
- R13 pad 1: +3V3 -> Net-(Q3-Pad1)
- R13 pad 2: /Audio/INSWITCH -> LED_1G_CTRL
- R14 pad 1: JD_IN -> Net-(Q4-Pad1)
- R14 pad 2: /Audio/INSWITCH -> LED_2G_CTRL
- R15 pad 1: /Audio/RSWITCH -> Net-(Q5-Pad1)
- R15 pad 2: +1.8V -> LED_1B_CTRL
- R16 pad 1: /Audio/HPSWITCH -> Net-(Q6-Pad1)
- R16 pad 2: +3V3 -> LED_2B_CTRL
- R17 pad 1: /Audio/LSWITCH -> +1V8
- R17 pad 2: +1.8V -> /Audio/INSWITCH
- R18 pad 1: (no net) -> JD_IN
- R18 pad 2: /Audio/HPSWITCH -> /Audio/INSWITCH
- R19 pad 1: JD_ROUT -> +5V
- R19 pad 2: /Audio/RSWITCH -> /Audio/LED_1RA
- R20 pad 1: JD_LOUT -> +5V
- R20 pad 2: /Audio/LSWITCH -> /Audio/LED_1GA
- R21 pad 1: I2C3v3_SCLK -> +5V
- R21 pad 2: +3V3 -> /Audio/LED_1BA
- R22 pad 1: I2C3v3_SDIN -> +5V
- R22 pad 2: +3V3 -> /Audio/LED_2RA
- R36 pad 1: +1.8V -> Net-(R36-Pad1)
- R36 pad 2: Net-(R36-Pad2) -> USBH_VBUS
- R38 pad 1: (no net) -> Net-(R38-Pad1)
- R41 pad 1: (no net) -> Net-(R41-Pad1)
- R43 pad 1: Net-(R43-Pad1) -> +1V8
- R43 pad 2: GND -> RF_IRQ
- R44 pad 1: DDR3_CK_P -> +1V8
- R44 pad 2: DDR3_CK_N -> TEMPO_SW
- R45 pad 1: Net-(R45-Pad1) -> +5V
- R45 pad 2: +1V35 -> /Sensors/TEMPO_LED_R
- SW1 pad 3: (no net) -> /Sensors/TEMPO_LED_D
- SW1 pad 4: (no net) -> /Sensors/TEMPO_LED_R
- U13 pad 10: (no net) -> I2C18_SCLK
- U13 pad 5: Net-(R36-Pad2) -> Net-(R42-Pad2)
- U13 pad 9: (no net) -> I2C18_SDIN
- U14 pad 1: (no net) -> I2C33_SDA
- U14 pad 7: (no net) -> I2C33_SCLK
- U15 pad L8: Net-(R40-Pad1) -> Net-(R46-Pad1)
- U6 pad 1: I2S_MCLK -> GND
- U6 pad 2: I2S_BCLK -> Net-(C21-Pad1)
- U6 pad 3: I2S_LRCLK -> Net-(C16-Pad1)
- U9 pad 1: (no net) -> I2S_MCLK
- U9 pad 2: (no net) -> I2S_BCLK
- U9 pad 3: GND -> I2S_LRCLK
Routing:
- net GND: track 0.00 -> 39.0 mm, vias 0 -> 68
- net +1V8: track 0.00 -> 11.3 mm, vias 0 -> 26
- net +1V0: track 0.00 -> 9.05 mm, vias 0 -> 15
- net +3V3: track 0.00 -> 5.09 mm, vias 0 -> 15
- net +1V35: track 0.00 -> 5.09 mm, vias 0 -> 9
- added copper zone on 1V8, net +1V8
- added copper zone on B.Cu, net +3V3
- added copper zone on F.Cu, net GND
- removed copper zone on Core_Supply_5V, net +1.0V
- removed copper zone on Core_Supply_5V, net +1.2V
- removed copper zone on B.Cu, net +1.8V
- removed copper zone on Core_Supply_5V, net +5V
- removed copper zone on GND0, net GND
- removed copper zone on GND1, net GND
- removed copper zone on SIGNAL1, net GND
- removed copper zone on SIGNAL2, net GND
- removed copper zone on SIGNAL3, net GND
- removed copper zone on F.Cu, net GNDA
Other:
- net class Analog removed
- net class Config removed
- net class Crystal removed
- net class DDR_Differential added: clearance 0.102, trace_width 0.13, via_dia 0.48, via_drill 0.25
- net class DDR_Single added: clearance 0.102, trace_width 0.13, via_dia 0.48, via_drill 0.25
- net class Default: via_dia 0.45 -> 0.48; via_drill 0.22 -> 0.25
- net class GPIF removed
- net class HDMI: via_dia 0.45 -> 0.48; via_drill 0.22 -> 0.25
- net class LEDs removed
- net class Peripherals removed
- net class Power: trace_width 0.39 -> 0.13; via_dia 0.7 -> 0.48; via_drill 0.4 -> 0.25
- net class UI removed
- net class USB SIG: via_dia 0.45 -> 0.48; via_drill 0.22 -> 0.25

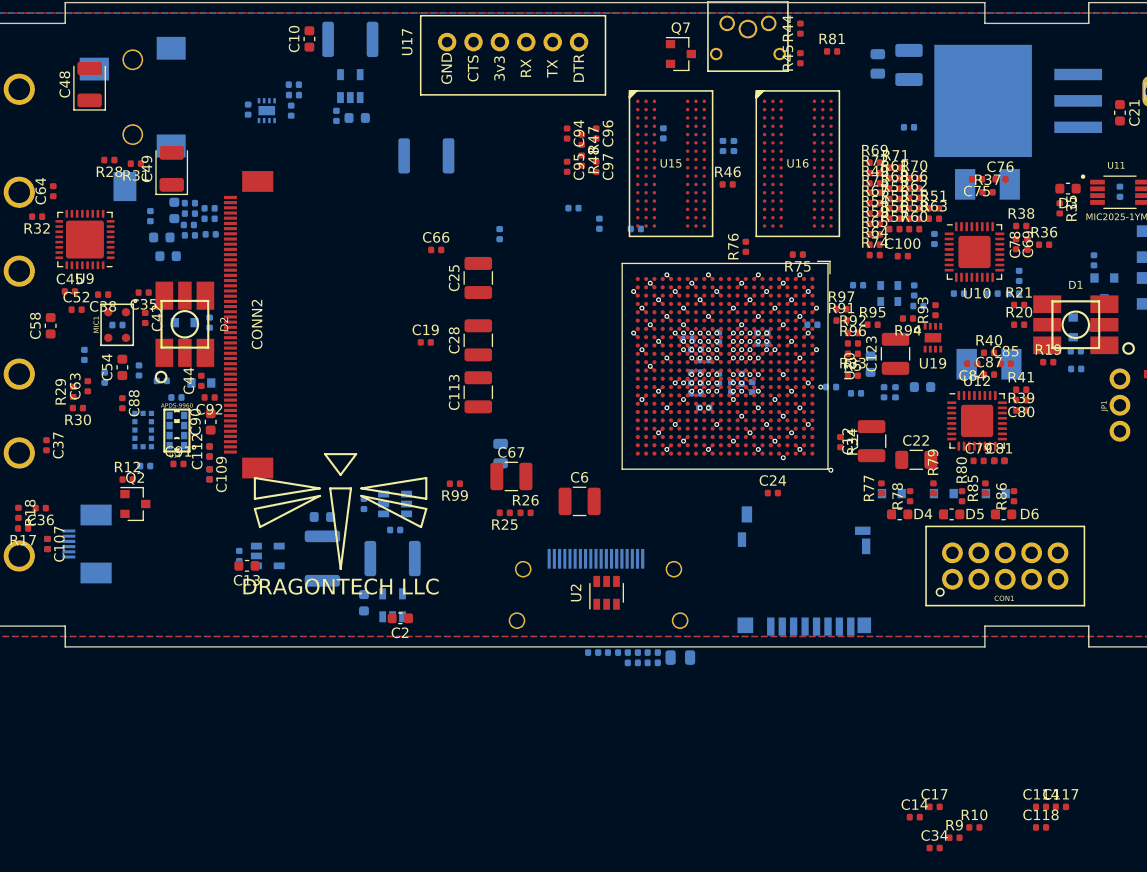
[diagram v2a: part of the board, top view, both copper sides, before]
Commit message: everything placed, about to shrink text size globally
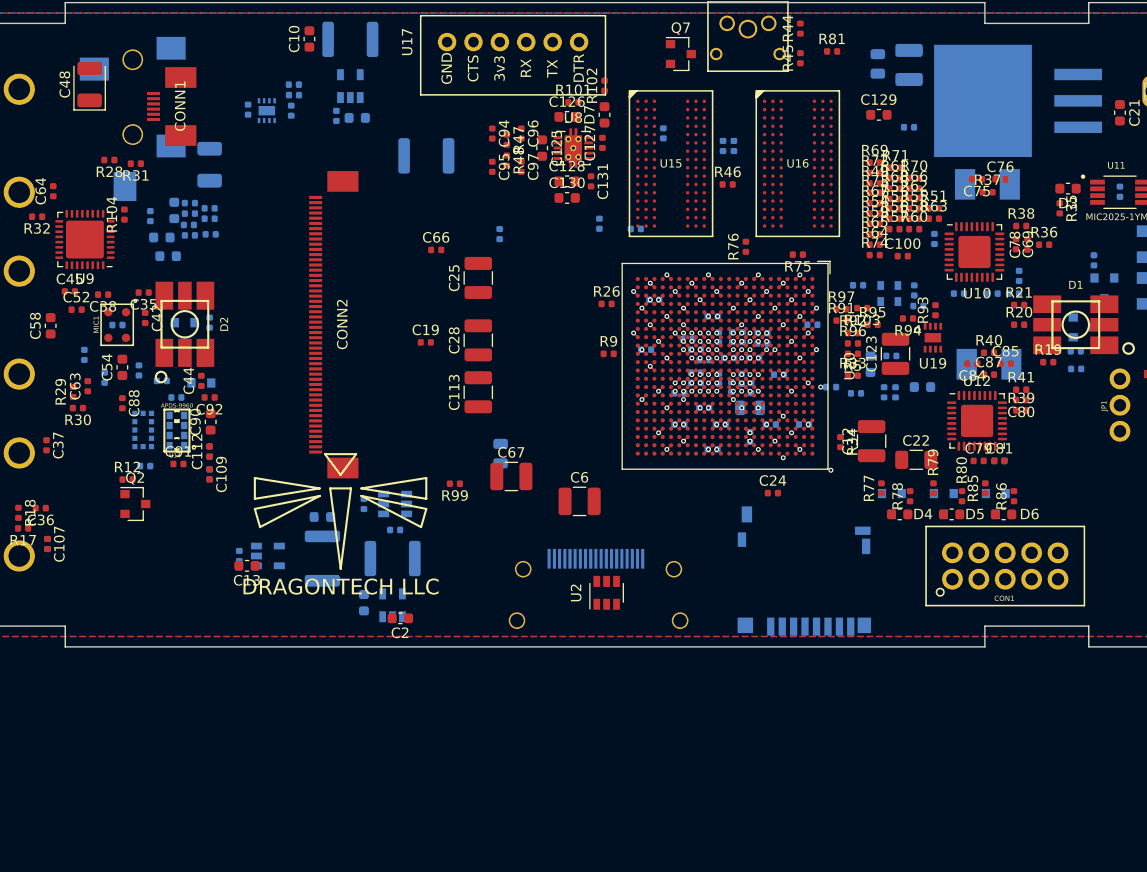
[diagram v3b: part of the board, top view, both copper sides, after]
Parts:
- added C125: 10uF, Capacitor_SMD:C_0603_1608Metric, F.Cu at (182.4, 107.0)
- added C126: 10uF, Capacitor_SMD:C_0603_1608Metric, F.Cu at (184.8, 104.0)
- added C127: 4.7uF, Capacitor_SMD:C_0402_1005Metric, F.Cu at (188.2, 106.5)
- added C128: 10uF, Capacitor_SMD:C_0603_1608Metric, F.Cu at (184.8, 110.2)
- added C129: 10uF, Capacitor_SMD:C_0603_1608Metric, F.Cu at (214.8, 103.8)
- added C130: 10uF, Capacitor_SMD:C_0603_1608Metric, F.Cu at (184.8, 111.8)
- added C131: .1uF, Capacitor_SMD:C_0402_1005Metric, F.Cu at (187.1, 110.2)
- added D7: BLUE LED, Capacitor_SMD:C_0603_1608Metric, F.Cu at (188.4, 103.8)
- added R101: 100k, Resistor_SMD:R_0402_1005Metric, F.Cu at (185.4, 102.6)
- added R102: 150, Resistor_SMD:R_0402_1005Metric, F.Cu at (188.4, 101.0)
- added R103: 4.7k, Resistor_SMD:R_0402_1005Metric, F.Cu at (213.2, 122.4)
- added R104: 4.7k, Resistor_SMD:R_0402_1005Metric, F.Cu at (142.2, 113.4)
- added U8: TPS51200DRCR, Package_SON:VSON-10-1EP_3x3mm_P0.5mm_EP1.65x2.4mm_ThermalVias, F.Cu at (185.4, 107.0)
- C114, C117, C118, C14, C17, C34, C49, R10, R25: moved to B.Cu
- CONN1: moved to F.Cu
- R50: value 100 -> 80.6 1%
- moved C118 59.6 mm to (192.4, 126.4)
- moved R9 57.2 mm to (188.8, 126.8)
- moved C117 54.6 mm to (201.7, 125.2), turned to 90 degrees
- moved R10 50.5 mm to (195.6, 130.6), turned to 180 degrees
- moved C34 47.5 mm to (216.0, 127.0)
- moved C17 47.5 mm to (200.4, 127.2)
- moved C14 46.8 mm to (202.8, 127.2), turned to 180 degrees
- moved C114 45.1 mm to (204.4, 133.6)
- moved CONN1 42.9 mm to (145.0, 103.0), turned to 90 degrees
- moved C59 31.1 mm to (205.2, 128.8)
- moved C46 26.3 mm to (207.6, 133.6), turned to 0 degrees
- moved C55 25.7 mm to (202.4, 134.8), turned to 90 degrees
- moved R25 25.1 mm to (193.2, 121.6)
- moved C61 24.9 mm to (202.4, 132.0), turned to 0 degrees
- moved C57 23.9 mm to (199.6, 133.6)
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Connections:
- C39 pad 2: +1V8 -> +3V3
- C41 pad 2: +1V8 -> +3V3
- R51 pad 2: +1V35 -> DDR3_VTT
- R52 pad 2: +1V35 -> DDR3_VTT
- R53 pad 2: +1V35 -> DDR3_VTT
- R54 pad 2: +1V35 -> DDR3_VTT
- R55 pad 2: +1V35 -> DDR3_VTT
- R56 pad 2: +1V35 -> DDR3_VTT
- R57 pad 2: +1V35 -> DDR3_VTT
- R58 pad 2: +1V35 -> DDR3_VTT
- R59 pad 2: +1V35 -> DDR3_VTT
- R60 pad 2: +1V35 -> DDR3_VTT
- R61 pad 2: +1V35 -> DDR3_VTT
- R62 pad 2: +1V35 -> DDR3_VTT
- R63 pad 2: +1V35 -> DDR3_VTT
- R64 pad 2: +1V35 -> DDR3_VTT
- R65 pad 2: +1V35 -> DDR3_VTT
- R66 pad 2: +1V35 -> DDR3_VTT
- R67 pad 2: +1V35 -> DDR3_VTT
- R68 pad 2: +1V35 -> DDR3_VTT
- R69 pad 2: +1V35 -> DDR3_VTT
- R70 pad 2: +1V35 -> DDR3_VTT
- R71 pad 2: +1V35 -> DDR3_VTT
- R72 pad 2: +1V35 -> DDR3_VTT
- R73 pad 2: +1V35 -> DDR3_VTT
- U20 pad AA18: (no net) -> HDMI_CLK_N
- U20 pad AA4: (no net) -> I2C18_SDIN
- U20 pad T22: HDMI_CLK_P -> HDMI_R_P
- U20 pad U16: (no net) -> DDR3_VTT_EN
- U20 pad U20: HDMI_B_P -> (no net)
- U20 pad U22: HDMI_CLK_N -> HDMI_R_N
- U20 pad V19: HDMI_CEC -> (no net)
- U20 pad V20: HDMI_B_N -> HDMI_CEC
- U20 pad V22: HDMI_R_P -> HDMI_G_P
- U20 pad W20: HDMI_G_P -> HDMI_B_P
- U20 pad W21: HDMI_G_N -> HDMI_B_N
- U20 pad W22: HDMI_R_N -> HDMI_G_N
- U20 pad Y18: JD_LOUT -> HDMI_CLK_P
- U20 pad Y19: (no net) -> JD_LOUT
- U20 pad Y4: (no net) -> I2C18_SCLK
- U9 pad 7: +1V8 -> +3V3
- U9 pad 8: I2C18_SCLK -> I2C33_SCLK
- U9 pad 9: I2C18_SDIN -> I2C33_SDIN
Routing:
- net INIT_B: track 0.00 -> 0.57 mm, vias 0 -> 1
- net I2C18_SCLK: track 0.00 -> 0.57 mm, vias 0 -> 1
- net GND: vias 68 -> 71
- net +3V3: vias 15 -> 17
- net +1V8: vias 26 -> 25
- net +1V0: vias 15 -> 17
